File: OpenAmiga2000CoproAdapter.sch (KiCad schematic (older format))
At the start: 7 parts, among them CN1 A2000_COPRO_SLOT, P1 CONN_2, P2 CONN_2, P3 CONN_2, P4 CONN_2, P99 OSHW_LOGO, U1 68000D

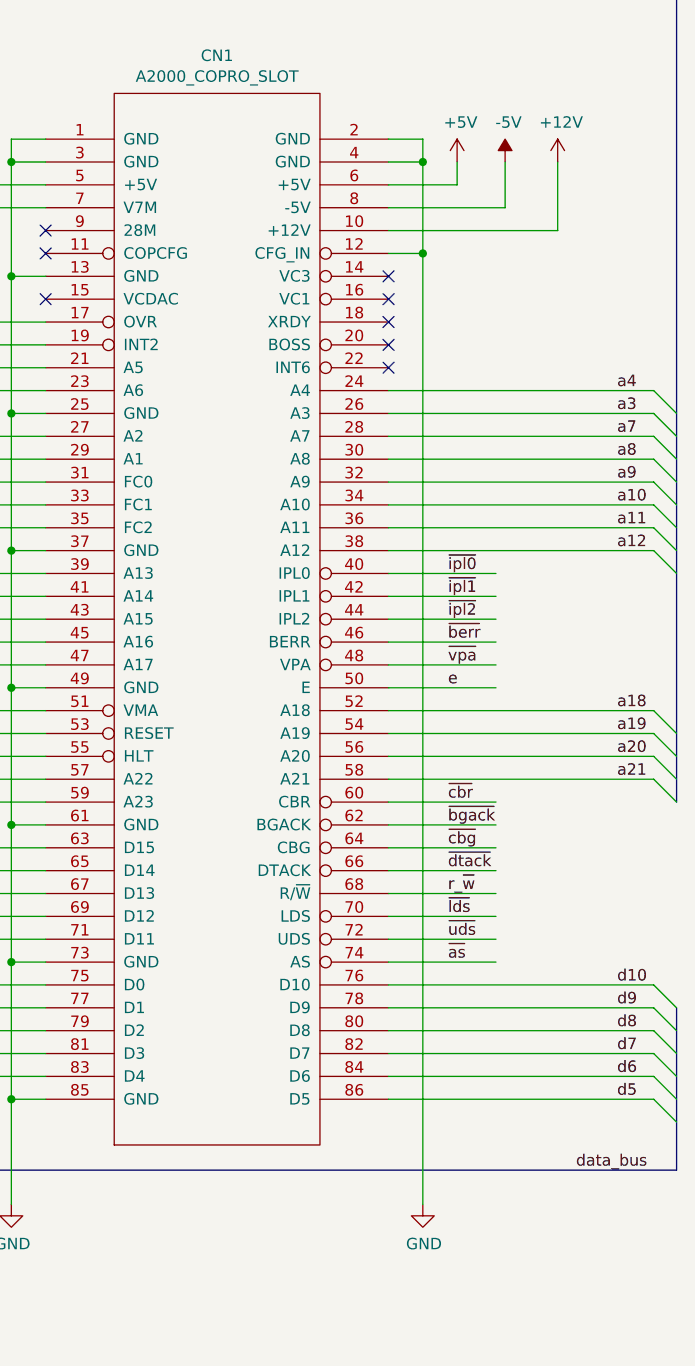
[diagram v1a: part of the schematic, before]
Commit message: Treat CONFIG_IN pin properly
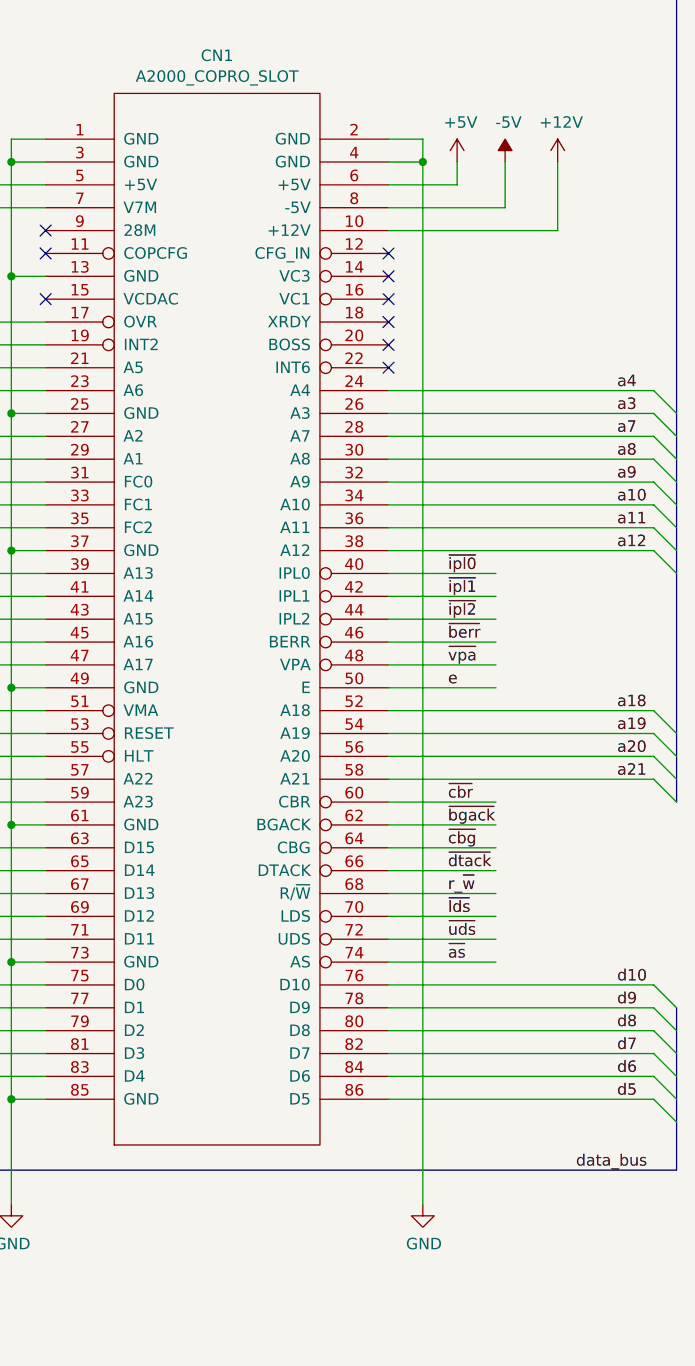
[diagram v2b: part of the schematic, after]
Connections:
- wire segments 177 -> 175
- no-connect marks 9 -> 10
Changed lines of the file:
@@
 Sheet 1 1
 Title "OpenAmiga2000CoproAdapter"
-Date "2019-02-11"
-Rev "1"
+Date "2019-02-14"
+Rev "2git"
 Comp "SukkoPera"
 Comment1 "Based on work by Kipper2K"
@@
 	1    0    0    -1
 $EndComp
-Wire Wire Line
-	9270 2090 9420 2090
-Connection ~ 9420 2090
 Wire Wire Line
 	9270 1690 9420 1690
@@
 Wire Wire Line
 	7620 5790 7620 6250
-Wire Wire Line
-	9420 2090 9420 6250
 Wire Bus Line
 	10530 900  6510 900
@@
 Text Label 7260 3290 0    50   ~ 0
 fc2
-Wire Wire Line
-	9420 1690 9420 2090
 Connection ~ 9420 1690
 $Comp
@@
 $EndComp
 NoConn ~ 6790 7530
+Wire Wire Line
+	9420 1690 9420 6250
+NoConn ~ 9270 2090
 Wire Bus Line
 	10530 5390 10530 6100

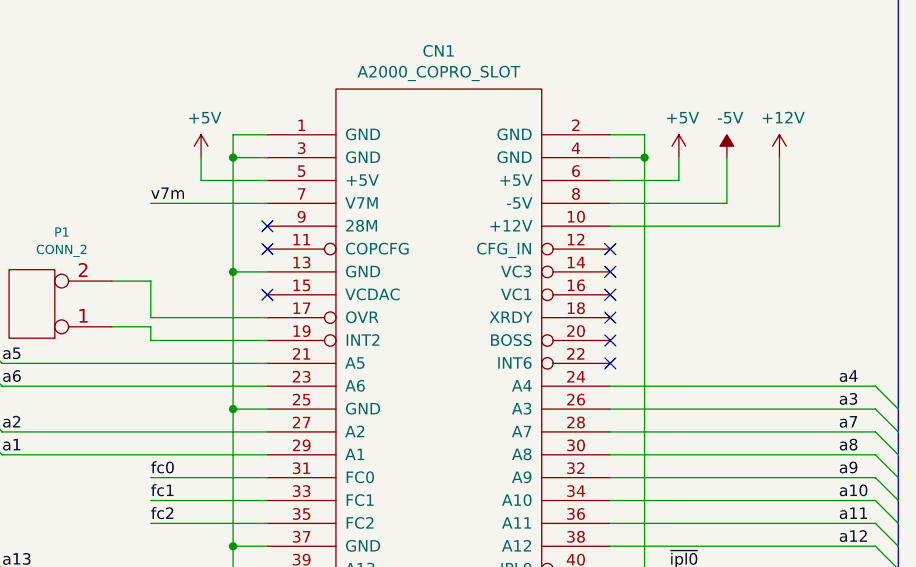
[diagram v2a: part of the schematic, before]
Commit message: Add test points for *all* the signals available on the connector
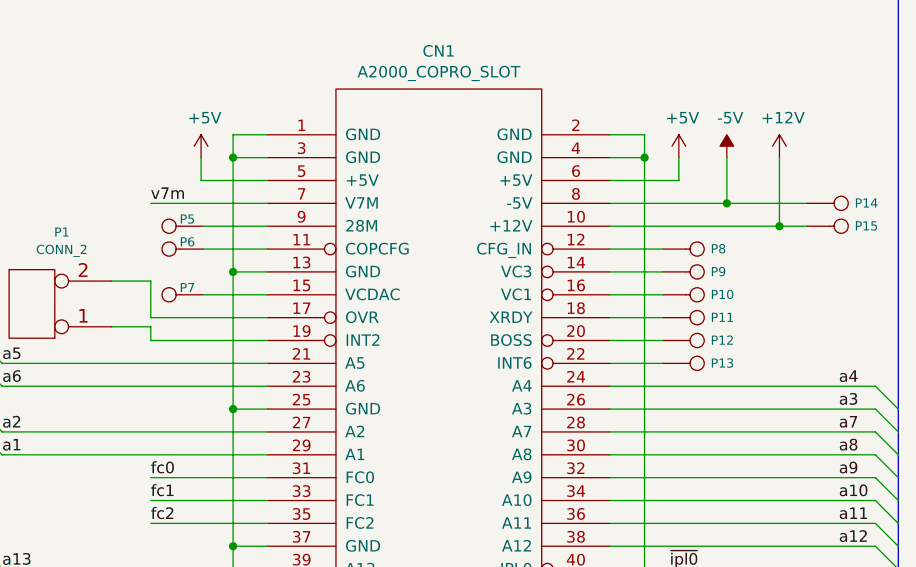
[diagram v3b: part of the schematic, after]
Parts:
- added P10, P11, P12, P13, P14, P15, P5, P6, P7, P8, P9: CONN_1, TestPoint:TestPoint_Pad_D1.5mm, symbol conn:CONN_1
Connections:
- wire segments 175 -> 186
- no-connect marks 10 -> 1
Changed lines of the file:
@@
 Text Label 10270 5790 0    50   ~ 0
 d5
-NoConn ~ 9270 2190
-NoConn ~ 9270 2290
-NoConn ~ 9270 2390
-NoConn ~ 9270 2490
-NoConn ~ 9270 2590
 $Comp
 L power:+5V #PWR01
@@
 Wire Wire Line
 	7480 1790 7770 1790
-NoConn ~ 7770 1990
-NoConn ~ 7770 2090
-NoConn ~ 7770 2290
 Wire Wire Line
 	7620 5790 7620 6250
@@
 Wire Wire Line
 	9420 1690 9420 6250
-NoConn ~ 9270 2090
+$Comp
+L conn:CONN_1 P8
+U 1 1 5C6A5338
+P 9650 2090
+F 0 "P8" H 9709 2090 40  0000 L CNN
+F 1 "CONN_1" H 9600 2130 30  0001 C CNN
+F 2 "TestPoint:TestPoint_Pad_D1.5mm" H 9650 2090 50  0001 C CNN
+F 3 "" H 9650 2090 50  0001 C CNN
+	1    9650 2090
+	1    0    0    -1
+$EndComp
+$Comp
+L conn:CONN_1 P9
+U 1 1 5C6A5554
+P 9650 2190
+F 0 "P9" H 9709 2190 40  0000 L CNN
+F 1 "CONN_1" H 9600 2230 30  0001 C CNN
+F 2 "TestPoint:TestPoint_Pad_D1.5mm" H 9650 2190 50  0001 C CNN
+F 3 "" H 9650 2190 50  0001 C CNN
+	1    9650 2190
+	1    0    0    -1
+$EndComp
+$Comp
+L conn:CONN_1 P10
+U 1 1 5C6A5637
+P 9650 2290
+F 0 "P10" H 9709 2290 40  0000 L CNN
+F 1 "CONN_1" H 9600 2330 30  0001 C CNN
+F 2 "TestPoint:TestPoint_Pad_D1.5mm" H 9650 2290 50  0001 C CNN
+F 3 "" H 9650 2290 50  0001 C CNN
+	1    9650 2290
+	1    0    0    -1
+$EndComp
+$Comp
+L conn:CONN_1 P11
+U 1 1 5C6A56D1
+P 9650 2390
+F 0 "P11" H 9709 2390 40  0000 L CNN
+F 1 "CONN_1" H 9600 2430 30  0001 C CNN
+F 2 "TestPoint:TestPoint_Pad_D1.5mm" H 9650 2390 50  0001 C CNN
+F 3 "" H 9650 2390 50  0001 C CNN
+	1    9650 2390
+	1    0    0    -1
+$EndComp
+$Comp
+L conn:CONN_1 P12
+U 1 1 5C6A5776
+P 9650 2490
+F 0 "P12" H 9709 2490 40  0000 L CNN
+F 1 "CONN_1" H 9600 2530 30  0001 C CNN
+F 2 "TestPoint:TestPoint_Pad_D1.5mm" H 9650 2490 50  0001 C CNN
+F 3 "" H 9650 2490 50  0001 C CNN
+	1    9650 2490
+	1    0    0    -1
+$EndComp
+$Comp
+L conn:CONN_1 P13
+U 1 1 5C6A57FA
+P 9650 2590
+F 0 "P13" H 9709 2590 40  0000 L CNN
+F 1 "CONN_1" H 9600 2630 30  0001 C CNN
+F 2 "TestPoint:TestPoint_Pad_D1.5mm" H 9650 2590 50  0001 C CNN
+F 3 "" H 9650 2590 50  0001 C CNN
+	1    9650 2590
+	1    0    0    -1
+$EndComp
+Wire Wire Line
+	9270 2090 9500 2090
+Wire Wire Line
+	9270 2190 9500 2190
+Wire Wire Line
+	9270 2290 9500 2290
+Wire Wire Line
+	9270 2390 9500 2390
+Wire Wire Line
+	9270 2490 9500 2490
+Wire Wire Line
+	9270 2590 9500 2590
+$Comp
+L conn:CONN_1 P5
+U 1 1 5C731E0D
+P 7340 1990
+F 0 "P5" H 7260 2020 40  0000 C CNN
+F 1 "CONN_1" H 7290 2030 30  0001 C CNN
+F 2 "TestPoint:TestPoint_Pad_D1.5mm" H 7340 1990 50  0001 C CNN
+F 3 "" H 7340 1990 50  0001 C CNN
+	1    7340 1990
+	-1   0    0    -1
+$EndComp
+$Comp
+L conn:CONN_1 P6
+U 1 1 5C73200C
+P 7340 2090
+F 0 "P6" H 7260 2120 40  0000 C CNN
+F 1 "CONN_1" H 7290 2130 30  0001 C CNN
+F 2 "TestPoint:TestPoint_Pad_D1.5mm" H 7340 2090 50  0001 C CNN
+F 3 "" H 7340 2090 50  0001 C CNN
+	1    7340 2090
+	-1   0    0    -1
+$EndComp
+$Comp
+L conn:CONN_1 P7
+U 1 1 5C7320AF
+P 7340 2290
+F 0 "P7" H 7260 2320 40  0000 C CNN
+F 1 "CONN_1" H 7290 2330 30  0001 C CNN
+F 2 "TestPoint:TestPoint_Pad_D1.5mm" H 7340 2290 50  0001 C CNN
+F 3 "" H 7340 2290 50  0001 C CNN
+	1    7340 2290
+	-1   0    0    -1
+$EndComp
+Wire Wire Line
+	7490 1990 7770 1990
+Wire Wire Line
+	7490 2090 7770 2090
+Wire Wire Line
+	7490 2290 7770 2290
+$Comp
+L conn:CONN_1 P15
+U 1 1 5C76E7B4
+P 10280 1990
+F 0 "P15" H 10339 1990 40  0000 L CNN
+F 1 "CONN_1" H 10230 2030 30  0001 C CNN
+F 2 "TestPoint:TestPoint_Pad_D1.5mm" H 10280 1990 50  0001 C CNN
+F 3 "" H 10280 1990 50  0001 C CNN
+	1    10280 1990
+	1    0    0    -1
+$EndComp
+$Comp
+L conn:CONN_1 P14
+U 1 1 5C76E822
+P 10280 1890
+F 0 "P14" H 10339 1890 40  0000 L CNN
+F 1 "CONN_1" H 10230 1930 30  0001 C CNN
+F 2 "TestPoint:TestPoint_Pad_D1.5mm" H 10280 1890 50  0001 C CNN
+F 3 "" H 10280 1890 50  0001 C CNN
+	1    10280 1890
+	1    0    0    -1
+$EndComp
+Wire Wire Line
+	9780 1890 10130 1890
+Connection ~ 9780 1890
+Wire Wire Line
+	10010 1990 10130 1990
 Wire Bus Line
 	10530 5390 10530 6100
@@
 Wire Bus Line
 	4960 3950 4960 5560
+Connection ~ 10010 1990
 $EndSCHEMATC

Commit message: Add jumpers for E, Boss
* Cutting the E jumper and closing the BOSS one will allow the card to work without removing the original cpu
* Closing BOSS is required for B2000 DMA to work, buster doesn't route BR to the copro slot unless /BOSS is asserted
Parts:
- removed P12: CONN_1, TestPoint:TestPoint_Pad_D1.5mm, symbol conn:CONN_1
- added P1: CONN_2, Jumper:SolderJumper-2_P1.3mm_Bridged_RoundedPad1.0x1.5mm, symbol OpenAmiga2000CoproAdapter-rescue:CONN_2-conn
- added P17: CONN_2, Jumper:SolderJumper-2_P1.3mm_Open_RoundedPad1.0x1.5mm, symbol OpenAmiga2000CoproAdapter-rescue:CONN_2-conn
- P10: renamed from P8; symbol conn:CONN_1 -> OpenAmiga2000CoproAdapter-rescue:CONN_1-conn
- P11: renamed from P9; symbol conn:CONN_1 -> OpenAmiga2000CoproAdapter-rescue:CONN_1-conn
- P12: renamed from P10; symbol conn:CONN_1 -> OpenAmiga2000CoproAdapter-rescue:CONN_1-conn
- P13: renamed from P11; symbol conn:CONN_1 -> OpenAmiga2000CoproAdapter-rescue:CONN_1-conn
- P14: renamed from P13; symbol conn:CONN_1 -> OpenAmiga2000CoproAdapter-rescue:CONN_1-conn
- P15: renamed from P14; symbol conn:CONN_1 -> OpenAmiga2000CoproAdapter-rescue:CONN_1-conn
- P16: renamed from P15; symbol conn:CONN_1 -> OpenAmiga2000CoproAdapter-rescue:CONN_1-conn
- P2, P3, P4: symbol conn:CONN_2 -> OpenAmiga2000CoproAdapter-rescue:CONN_2-conn
- P5: renamed from P1; symbol conn:CONN_2 -> OpenAmiga2000CoproAdapter-rescue:CONN_2-conn
- P6: renamed from P99; symbol conn:CONN_1 -> OpenAmiga2000CoproAdapter-rescue:CONN_1-conn
- P7: renamed from P5; symbol conn:CONN_1 -> OpenAmiga2000CoproAdapter-rescue:CONN_1-conn
- P8: renamed from P6; symbol conn:CONN_1 -> OpenAmiga2000CoproAdapter-rescue:CONN_1-conn
- P9: renamed from P7; symbol conn:CONN_1 -> OpenAmiga2000CoproAdapter-rescue:CONN_1-conn
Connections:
- wire segments 186 -> 188
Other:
- moved on the sheet: P10, P11, P12, P13, P14
